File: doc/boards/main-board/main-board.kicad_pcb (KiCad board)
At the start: 2 copper layers, 65 x 100 mm, 117 parts, among them P1 Raspberry_Pi_2_3, P10 ROTENC 7 SW, P11 ROTENC 1, P12 ROTENC 2, P13 ROTENC 3, P14 ROTENC 4, P15 ROTENC 5, P16 DISPLAY, P2 FOOTSW, P3 NAV SW, P4 AUDIO BOARD, P5 LEDS, P6 EXPR 0, P7 EXPR 1, P8 EXPR 2, P9 ROTENC 6 SW, Q1 BC547, Q2 BC547, Q3 BC547, U1 MCP3008, U3 MCP23017, U4 MCP23017

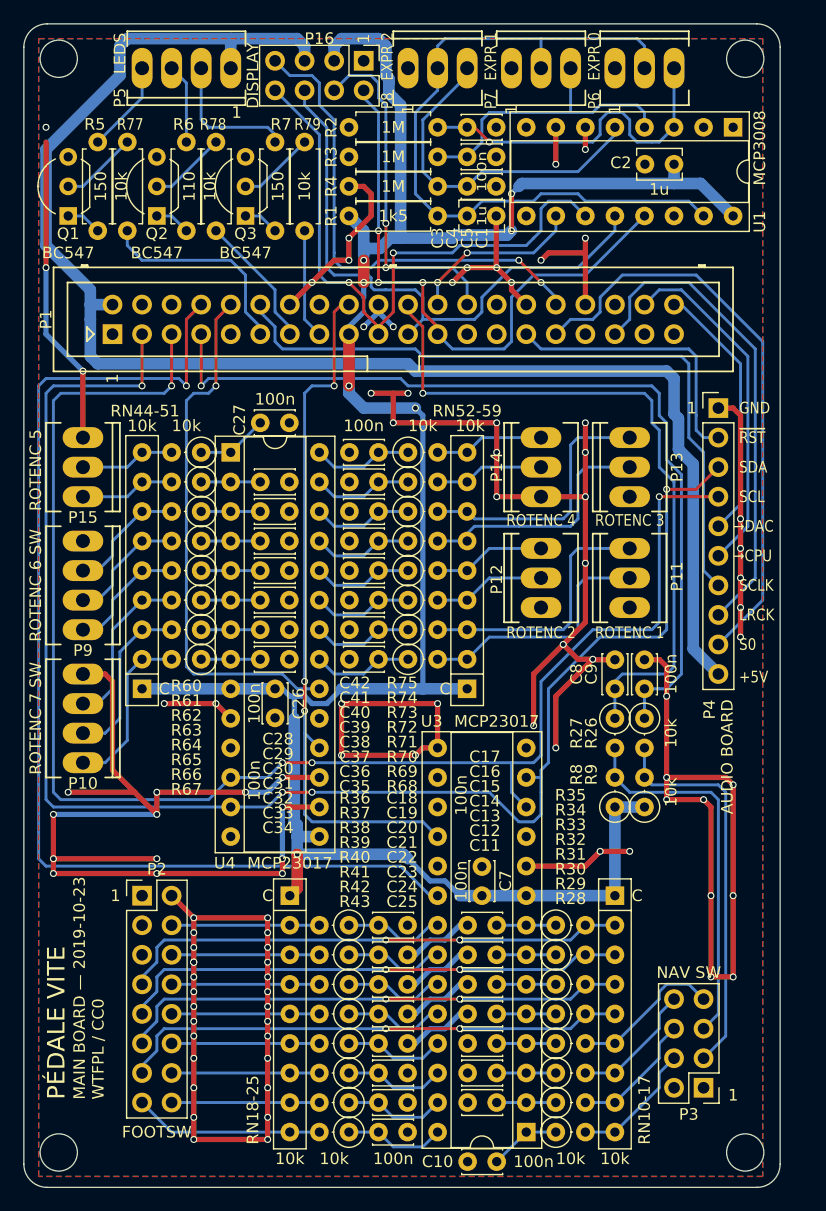
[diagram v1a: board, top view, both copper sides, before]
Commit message: Updated board files to KiCAD 6
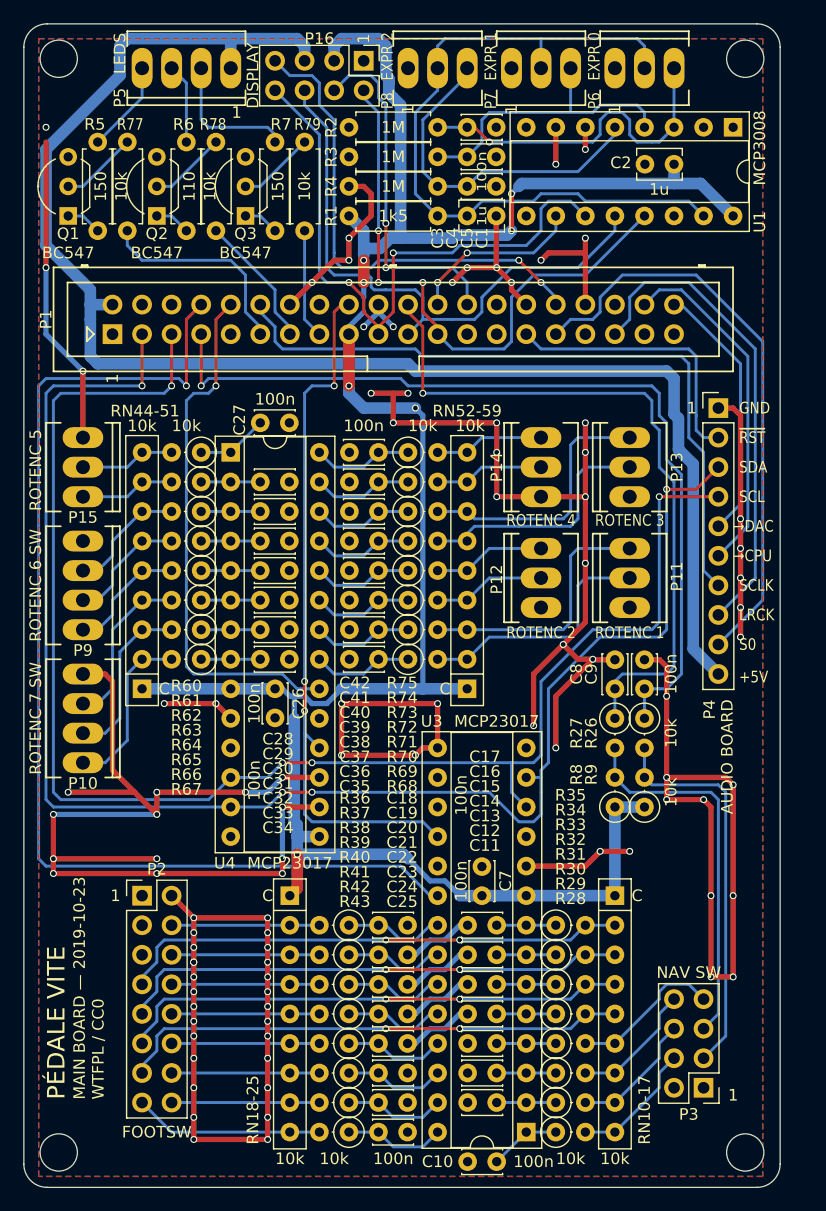
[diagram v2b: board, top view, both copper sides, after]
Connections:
- net ~CODEC_RESET renamed ~{CODEC_RESET}
- net ~Reset renamed ~{Reset}
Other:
- net class Default removed
- net class Power removed
- board text added: "~{RST}"
- board text removed: "~RST"
